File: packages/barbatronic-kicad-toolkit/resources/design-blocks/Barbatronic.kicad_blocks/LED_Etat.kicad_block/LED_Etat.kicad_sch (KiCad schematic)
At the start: 2 parts

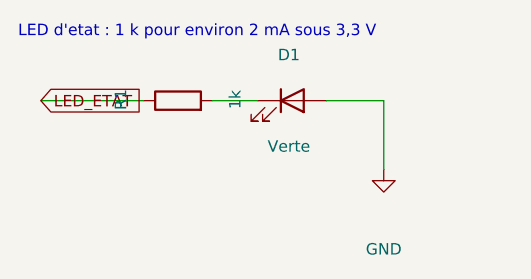
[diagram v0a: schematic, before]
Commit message: Sync docs with hand-edited design blocks
Entree_Alim_Protegee is gone, Servos_x4 is now the reusable single-
output Servos, and Regul_5V is new (78E05, needs the SparkFun PCM
power-symbols package for one symbol). Blocks are now maintained by
hand in KiCad, not generated.

Guard make_design_blocks.py behind --force: it wipes and rebuilds
the whole block library from a now-stale list, which would have
silently destroyed these edits on next run.
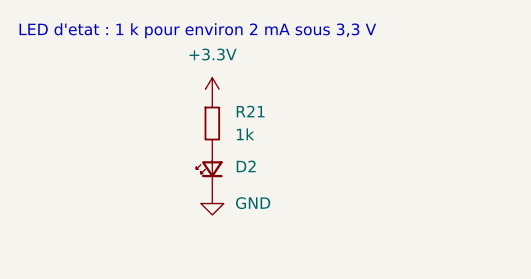
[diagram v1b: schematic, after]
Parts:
- removed D1: Verte, LED_SMD:LED_0805_2012Metric, symbol Device:LED
- removed R1: 1k, Resistor_SMD:R_0805_2012Metric, symbol Device:R
- added D2: LED_Small, LED_SMD:LED_1206_3216Metric_Pad1.42x1.75mm_HandSolder, symbol Device:LED_Small
- added R21: 1k, Resistor_SMD:R_1206_3216Metric_Pad1.30x1.75mm_HandSolder, symbol Device:R_Small
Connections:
- net GND: now also D2.1 (K)
- new net: D2.2 (A), R21.2
- new net +3.3V: R21.1
